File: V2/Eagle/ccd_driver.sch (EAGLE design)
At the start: 60 parts, among them J3 POWER_JACK, Q1 1A/60V/2.4Ω, Q2 BC214, U10 TPD4S012DRYR, U11 0ZCJ0050FF2G, U2 MK02FN128VLF10, U5 CP2102N-A01-GQFN20R

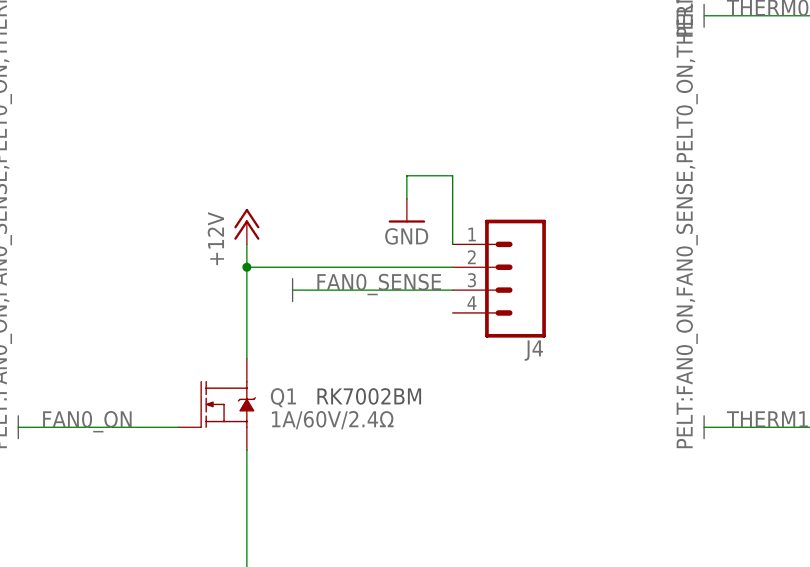
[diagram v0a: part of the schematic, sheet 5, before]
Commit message: changed jst fan connector
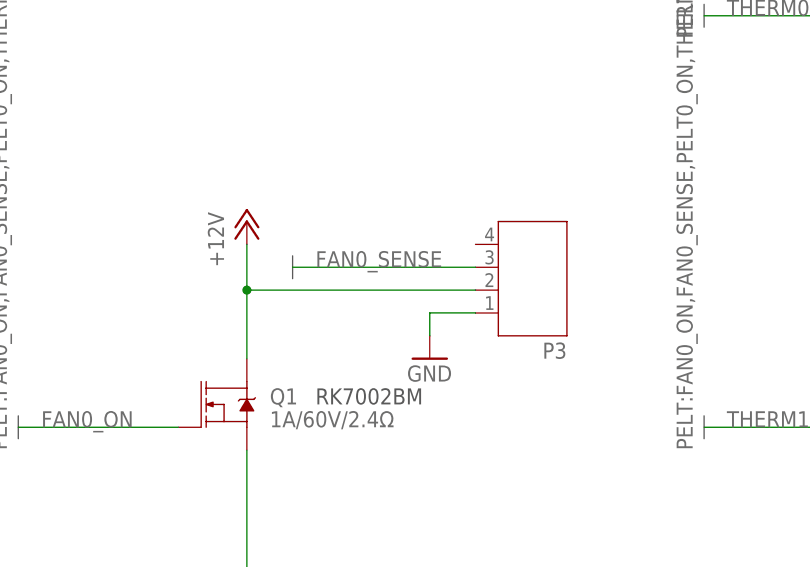
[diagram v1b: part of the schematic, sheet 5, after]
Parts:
- removed J4: (no value), SparkFun-Connectors:CONN_04JST-PTH
- added P3: (no value), jst-ph:JST-PH4
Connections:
- removed net FAN0_SENSE: J4.3
- net +12V: no longer J4.2
- net GND: now also P3.1; no longer J4.1
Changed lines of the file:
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@@
 <part name="GND8" library="supply1" library_urn="urn:adsk.eagle:library:371" deviceset="GND" device=""/>
 <part name="Q1" library="SparkFun-DiscreteSemi" library_urn="urn:adsk.eagle:library:514" deviceset="MOSFET-NCH" device="-BSS138" package3d_urn="urn:adsk.eagle:package:38446/1" value="1A/60V/2.4Ω"/>
-<part name="J4" library="SparkFun-Connectors" library_urn="urn:adsk.eagle:library:513" deviceset="CONN_04" device="JST-PTH" package3d_urn="urn:adsk.eagle:package:38101/1"/>
 <part name="GND11" library="supply1" library_urn="urn:adsk.eagle:library:371" deviceset="GND" device=""/>
 <part name="P+2" library="supply1" library_urn="urn:adsk.eagle:library:371" deviceset="+12V" device=""/>
@@
 <part name="R5" library="audio amplifier example" library_urn="urn:adsk.eagle:library:970892" deviceset="R-US_" device="R0603" package3d_urn="urn:adsk.eagle:package:970938/2" value="100k, 1%"/>
 <part name="GND19" library="supply1" library_urn="urn:adsk.eagle:library:371" deviceset="GND" device=""/>
+<part name="P3" library="jst-ph" deviceset="JST-PH4" device=""/>
 </parts>
 <sheets>
@@
 <instance part="GND8" gate="1" x="139.7" y="58.42"/>
 <instance part="Q1" gate="NMOS" x="137.16" y="86.36"/>
-<instance part="J4" gate="G$1" x="167.64" y="101.6" rot="R180"/>
-<instance part="GND11" gate="1" x="157.48" y="106.68"/>
+<instance part="GND11" gate="1" x="160.02" y="91.44"/>
 <instance part="P+2" gate="1" x="139.7" y="106.68"/>
 <instance part="P1" gate="G$1" x="218.44" y="129.54" rot="R180"/>
@@
 <instance part="R5" gate="G$1" x="205.74" y="73.66" rot="R90"/>
 <instance part="GND19" gate="1" x="205.74" y="60.96"/>
+<instance part="P3" gate="A" x="172.72" y="99.06" rot="R180"/>
 </instances>
 <busses>
@@
 </segment>
 <segment>
-<wire x1="144.78" y1="100.33" x2="144.78" y2="97.79" width="0.762" layer="92"/>
+<wire x1="144.78" y1="102.87" x2="144.78" y2="100.33" width="0.762" layer="92"/>
 </segment>
 <segment>
@@
 </segment>
 <segment>
-<pinref part="J4" gate="G$1" pin="1"/>
-<wire x1="162.56" y1="104.14" x2="162.56" y2="111.76" width="0.1524" layer="91"/>
-<wire x1="162.56" y1="111.76" x2="157.48" y2="111.76" width="0.1524" layer="91"/>
-<wire x1="157.48" y1="111.76" x2="157.48" y2="109.22" width="0.1524" layer="91"/>
+<wire x1="165.1" y1="96.52" x2="160.02" y2="96.52" width="0.1524" layer="91"/>
+<wire x1="160.02" y1="96.52" x2="160.02" y2="93.98" width="0.1524" layer="91"/>
 <pinref part="GND11" gate="1" pin="GND"/>
+<pinref part="P3" gate="A" pin="1"/>
 </segment>
 <segment>
@@
 </segment>
 <segment>
-<pinref part="J4" gate="G$1" pin="2"/>
 <pinref part="Q1" gate="NMOS" pin="D"/>
-<wire x1="162.56" y1="101.6" x2="139.7" y2="101.6" width="0.1524" layer="91"/>
-<wire x1="139.7" y1="101.6" x2="139.7" y2="91.44" width="0.1524" layer="91"/>
+<wire x1="165.1" y1="99.06" x2="139.7" y2="99.06" width="0.1524" layer="91"/>
+<wire x1="139.7" y1="99.06" x2="139.7" y2="91.44" width="0.1524" layer="91"/>
 <pinref part="P+2" gate="1" pin="+12V"/>
-<wire x1="139.7" y1="101.6" x2="139.7" y2="104.14" width="0.1524" layer="91"/>
-<junction x="139.7" y="101.6"/>
+<wire x1="139.7" y1="99.06" x2="139.7" y2="104.14" width="0.1524" layer="91"/>
+<junction x="139.7" y="99.06"/>
 </segment>
 </net>
 <net name="FAN0_SENSE" class="0">
 <segment>
-<pinref part="J4" gate="G$1" pin="3"/>
-<wire x1="162.56" y1="99.06" x2="144.78" y2="99.06" width="0.1524" layer="91"/>
-<label x="147.32" y="99.06" size="1.778" layer="95"/>
-</segment>
-<segment>
+<wire x1="165.1" y1="101.6" x2="144.78" y2="101.6" width="0.1524" layer="91"/>
+<label x="147.32" y="101.6" size="1.778" layer="95"/>
+</segment>
+<segment>

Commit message: added TFT screen + encoder, small cleanup, doubled peltier driver
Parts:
- added 1410460C1: 100uH, DMN1019UVT:1410460C
- added C14, C15, C8: 100nF, SparkFun-Capacitors:10PF-50V-5%(0603)
- added C16, C7: 10uF, SparkFun-Capacitors:10PF-50V-5%(0603)
- added C3: 47uF, SparkFun-Capacitors:10UF-1210-50V-20%
- added J4: (no value), SparkFun-Connectors:CONN_022.54MM_SCREWTERM
- added P4: (no value), jst-ph:JST-PH2
- added Q3: 2N2222, transistor:MMBT2222ALT1-NPN-SOT23-BEC
- added R10: 1k, audio amplifier example:R-US_R0603
- added R11, R12, R13, R14, R9: 10k, audio amplifier example:R-US_R0603
- added R15: 22 ohm, adafruit:R-US_R0805
- added R17: 1K, adafruit:R-US_R0805
- added R6: 100k, 1%, audio amplifier example:R-US_R0603
- added R7, R8: 220, audio amplifier example:R-US_R0603
- added S3: ENCODER-2LED, SparkFun-Switches:ENCODER-2LED
- added U$1: DMN1019UVT, DMN1019UVT:DMN1019UVT
- added U$10: JD-T1800, adafruit:JD-T1800
- added U$9: DB2431200L, DMN1019UVT:DB2431200L
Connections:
- net SD_DO renamed SPI_DO
- removed net SD_CLK: U$3.CLK
- removed net SD_DI: U$3.CMD_DIN
- new net CODE_A: C14.2, R13.1
- new net CODE_B: C8.1, R11.1
- new net CODE_BUTTON: C7.2, R10.2, R9.2
- new net CODE_LED_G: R8.1
- new net CODE_LED_R: R7.1
- new net FAN0_SENSE: P3.3
- new net LCD_BACKLIGHT: R17.2
- new net N$1: 1410460C1.2, C3.2, J4.2
- new net N$10: R13.2, R14.2, S3.A
- new net N$2: 1410460C1.1, U$1.D, U$9.+
- new net N$20: R11.2, R12.2, S3.B
- new net N$22: R15.1, U$10.LEDK
- new net N$23: Q3.C, R15.2
- new net N$24: Q3.B, R17.1
- new net N$3: R7.2, S3.+R
- new net N$5: R18.1
- new net N$8: R8.2, S3.+G
- new net N$9: R10.1, S3.SW
- new net PELT1_ON: U$1.G
- new net SPI_CLK: U$10.CLOCK, U$3.CLK
- new net SPI_DI: U$10.DATA, U$3.CMD_DIN
- new net TFT_CS: U$10.CS
- new net TFT_DC: U$10.RS/DC
- new net TFT_RESET: U$10.RESET
- net +12V: now also C3.1, J4.1, P3.2, U$9.-
- net 3.3V: now also C15.1, C16.1, P4.2, R12.1, R14.1, R9.1, U$10.LEDA, U$10.VCC, U$10.VCC2
- net GND: now also C14.1, C15.2, C16.2, C7.1, C8.2, Q3.E, R6.1, S3.-, S3.C, U$1.S, U$10.GND, U$10.GND1, U$10.GND2; no longer R18.1
- net THERM1: now also P4.1, R6.2
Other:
- note added: "CCD + AMP"
- note added: "DC selects whether data is command or to be stored in image ram"
- note added: "Main MCU"
- note added: "Peltier Cooler Driver + Thermistor + Fan"
- note added: "TFT Screen + Encoder"
- note added: "TFT-Screen + Encoder"
- note added: "TODO: Add power monitor for peltier"
- note added: "TODO: Add some sort of LCD interface + encoder [X]"
- note added: "TODO: Change resistors/caps to 0603"
- note added: "TODO: Halogen lamp drivers - Future PCB"
- note added: "TODO: LED Drivers - Future PCB"
- note removed: "TODO: Add some sort of LCD interface + encoder"
- note removed: "TODO: Change resistors to 0603"
- note removed: "TODO: Halogen lamp drivers"
- note removed: "TODO: LED Drivers"

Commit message: added my name to sch
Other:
- note added: "Jacob Booth"
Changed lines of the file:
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@@
 <text x="205.74" y="11.43" size="2.54" layer="97">Main MCU</text>
 <text x="7.62" y="142.24" size="1.778" layer="97" ratio="7">TODO: Add power monitor for peltier</text>
+<text x="252.73" y="17.78" size="2.54" layer="97">Jacob Booth</text>
 </plain>
 <instances>
@@
 <text x="7.62" y="200.66" size="6.4516" layer="97">CCD &amp; Amp</text>
 <text x="205.74" y="11.43" size="2.54" layer="97">CCD + AMP</text>
+<text x="252.73" y="17.78" size="2.54" layer="97">Jacob Booth</text>
 </plain>
 <instances>
@@
 <text x="7.62" y="200.66" size="6.4516" layer="97">USB</text>
 <text x="204.47" y="11.43" size="2.54" layer="97">USB</text>
+<text x="254" y="17.78" size="2.54" layer="97">Jacob Booth</text>
 </plain>
 <instances>
@@
 <text x="7.62" y="200.66" size="6.4516" layer="97">SD Card</text>
 <text x="205.74" y="11.43" size="2.54" layer="97">SD Card</text>
+<text x="252.73" y="17.78" size="2.54" layer="97">Jacob Booth</text>
 </plain>
 <instances>
@@
 <text x="205.74" y="7.62" size="2.54" layer="97">Peltier Cooler Driver + Thermistor
 + Fan</text>
+<text x="252.73" y="17.78" size="2.54" layer="97">Jacob Booth</text>
 </plain>
 <instances>
@@
 <text x="7.62" y="200.66" size="6.4516" layer="97">Power</text>
 <text x="205.74" y="11.43" size="2.54" layer="97">Power</text>
+<text x="252.73" y="17.78" size="2.54" layer="97">Jacob Booth</text>
 </plain>
 <instances>
@@
 <text x="223.52" y="154.94" size="1.778" layer="97">DC selects whether data is command
  or to be stored in image ram</text>
+<text x="252.73" y="17.78" size="2.54" layer="97">Jacob Booth</text>
 </plain>
 <instances>
